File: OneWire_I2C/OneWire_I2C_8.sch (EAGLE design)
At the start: 17 parts

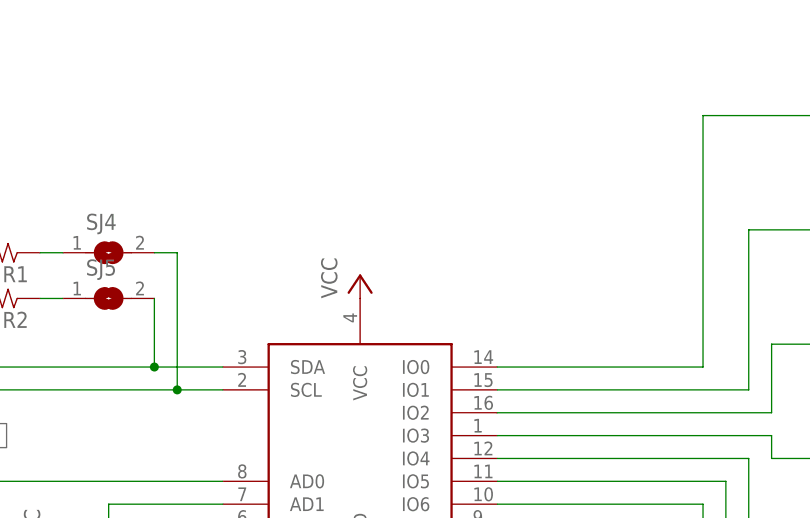
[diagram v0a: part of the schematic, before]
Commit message: Tweaks to I2C 1Wire bridge boards
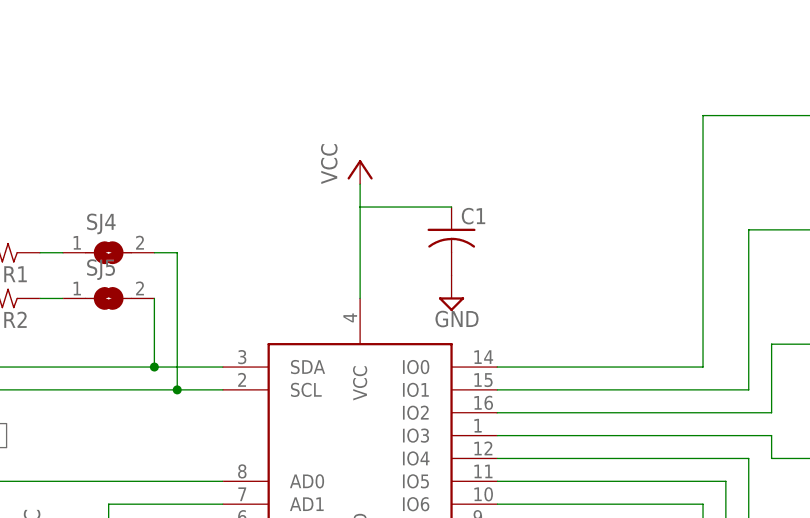
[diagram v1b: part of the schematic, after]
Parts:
- added C1: (no value), resistor:C-USC0603
- renumbered U$1 to W1
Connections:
- net GND: now also C1.2
- net VCC: now also C1.1
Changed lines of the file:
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@@
 <parts>
 <part name="FRAME1" library="frames" deviceset="LETTER_L" device=""/>
-<part name="U$1" library="Puffin" deviceset="DS2482-800" device=""/>
+<part name="W1" library="Puffin" deviceset="DS2482-800" device=""/>
 <part name="J1" library="SparkFun-Connectors" deviceset="M03" device="PTH"/>
 <part name="J2" library="SparkFun-Connectors" deviceset="M03" device="PTH"/>
@@
 <part name="SJ4" library="jumper" deviceset="SJ" device=""/>
 <part name="SJ5" library="jumper" deviceset="SJ" device=""/>
+<part name="C1" library="resistor" deviceset="C-US" device="C0603"/>
+<part name="SUPPLY2" library="supply2" deviceset="GND" device=""/>
 </parts>
 <sheets>
@@
 <instance part="FRAME1" gate="G$1" x="0" y="0"/>
 <instance part="FRAME1" gate="G$2" x="147.32" y="0"/>
-<instance part="U$1" gate="G$1" x="121.92" y="106.68"/>
+<instance part="W1" gate="G$1" x="121.92" y="106.68"/>
 <instance part="J1" gate="J$1" x="195.58" y="149.86" rot="R180"/>
 <instance part="J2" gate="J$1" x="195.58" y="137.16" rot="R180"/>
@@
 <instance part="SJ2" gate="G$1" x="81.28" y="88.9" rot="R270"/>
 <instance part="SJ3" gate="G$1" x="81.28" y="78.74" rot="R270"/>
-<instance part="VCC" gate="VCC" x="121.92" y="132.08"/>
+<instance part="VCC" gate="VCC" x="121.92" y="144.78"/>
 <instance part="P+2" gate="VCC" x="180.34" y="157.48"/>
 <instance part="P+3" gate="VCC" x="71.12" y="142.24"/>
@@
 <instance part="SJ4" gate="1" x="93.98" y="134.62"/>
 <instance part="SJ5" gate="1" x="93.98" y="129.54"/>
+<instance part="C1" gate="G$1" x="132.08" y="137.16"/>
+<instance part="SUPPLY2" gate="GND" x="132.08" y="129.54"/>
 </instances>
 <busses>
@@
 <net name="IO0" class="0">
 <segment>
-<pinref part="U$1" gate="G$1" pin="IO0"/>
+<pinref part="W1" gate="G$1" pin="IO0"/>
 <wire x1="137.16" y1="121.92" x2="160.02" y2="121.92" width="0.1524" layer="91"/>
 <wire x1="160.02" y1="121.92" x2="160.02" y2="149.86" width="0.1524" layer="91"/>
@@
 <net name="IO1" class="0">
 <segment>
-<pinref part="U$1" gate="G$1" pin="IO1"/>
+<pinref part="W1" gate="G$1" pin="IO1"/>
 <wire x1="137.16" y1="119.38" x2="165.1" y2="119.38" width="0.1524" layer="91"/>
 <wire x1="165.1" y1="119.38" x2="165.1" y2="137.16" width="0.1524" layer="91"/>
@@
 <net name="IO2" class="0">
 <segment>
-<pinref part="U$1" gate="G$1" pin="IO2"/>
+<pinref part="W1" gate="G$1" pin="IO2"/>
 <wire x1="137.16" y1="116.84" x2="167.64" y2="116.84" width="0.1524" layer="91"/>
 <wire x1="167.64" y1="116.84" x2="167.64" y2="124.46" width="0.1524" layer="91"/>
@@
 <net name="IO3" class="0">
 <segment>
-<pinref part="U$1" gate="G$1" pin="IO3"/>
+<pinref part="W1" gate="G$1" pin="IO3"/>
 <wire x1="137.16" y1="114.3" x2="167.64" y2="114.3" width="0.1524" layer="91"/>
 <wire x1="167.64" y1="114.3" x2="167.64" y2="111.76" width="0.1524" layer="91"/>
@@
 <net name="IO4" class="0">
 <segment>
-<pinref part="U$1" gate="G$1" pin="IO4"/>
+<pinref part="W1" gate="G$1" pin="IO4"/>
 <wire x1="137.16" y1="111.76" x2="165.1" y2="111.76" width="0.1524" layer="91"/>
 <wire x1="165.1" y1="111.76" x2="165.1" y2="99.06" width="0.1524" layer="91"/>
@@
 <net name="IO5" class="0">
 <segment>
-<pinref part="U$1" gate="G$1" pin="IO5"/>
+<pinref part="W1" gate="G$1" pin="IO5"/>
 <wire x1="137.16" y1="109.22" x2="162.56" y2="109.22" width="0.1524" layer="91"/>
 <wire x1="162.56" y1="109.22" x2="162.56" y2="86.36" width="0.1524" layer="91"/>
@@
 <net name="IO6" class="0">
 <segment>
-<pinref part="U$1" gate="G$1" pin="IO6"/>
+<pinref part="W1" gate="G$1" pin="IO6"/>
 <wire x1="137.16" y1="106.68" x2="160.02" y2="106.68" width="0.1524" layer="91"/>
 <wire x1="160.02" y1="106.68" x2="160.02" y2="73.66" width="0.1524" layer="91"/>
@@
 <net name="IO7" class="0">
 <segment>
-<pinref part="U$1" gate="G$1" pin="IO7"/>
+<pinref part="W1" gate="G$1" pin="IO7"/>
 <wire x1="137.16" y1="104.14" x2="157.48" y2="104.14" width="0.1524" layer="91"/>
 <wire x1="157.48" y1="104.14" x2="157.48" y2="60.96" width="0.1524" layer="91"/>
@@
 <net name="GND" class="0">
 <segment>
-<pinref part="U$1" gate="G$1" pin="GND"/>
+<pinref part="W1" gate="G$1" pin="GND"/>
 <pinref part="GND" gate="GND" pin="GND"/>
 </segment>
@@
 <junction x="182.88" y="58.42"/>
 </segment>
+<segment>
+<pinref part="C1" gate="G$1" pin="2"/>
+<pinref part="SUPPLY2" gate="GND" pin="GND"/>
+</segment>
 </net>
 <net name="VCC" class="0">
 <segment>
-<pinref part="U$1" gate="G$1" pin="VCC"/>
+<pinref part="W1" gate="G$1" pin="VCC"/>
 <pinref part="VCC" gate="VCC" pin="VCC"/>
+<wire x1="121.92" y1="142.24" x2="121.92" y2="139.7" width="0.1524" layer="91"/>
+<pinref part="C1" gate="G$1" pin="1"/>
+<wire x1="121.92" y1="139.7" x2="121.92" y2="129.54" width="0.1524" layer="91"/>
+<wire x1="132.08" y1="139.7" x2="121.92" y2="139.7" width="0.1524" layer="91"/>
 </segment>
 <segment>
@@
 <net name="AD0" class="0">
 <segment>
-<pinref part="U$1" gate="G$1" pin="AD0"/>
+<pinref part="W1" gate="G$1" pin="AD0"/>
 <pinref part="SJ1" gate="G$1" pin="2"/>
 <wire x1="106.68" y1="109.22" x2="81.28" y2="109.22" width="0.1524" layer="91"/>
@@
 <wire x1="81.28" y1="93.98" x2="93.98" y2="93.98" width="0.1524" layer="91"/>
 <wire x1="93.98" y1="93.98" x2="93.98" y2="106.68" width="0.1524" layer="91"/>
-<pinref part="U$1" gate="G$1" pin="AD1"/>
+<pinref part="W1" gate="G$1" pin="AD1"/>
 <wire x1="93.98" y1="106.68" x2="106.68" y2="106.68" width="0.1524" layer="91"/>
 </segment>
@@
 <wire x1="81.28" y1="83.82" x2="96.52" y2="83.82" width="0.1524" layer="91"/>
 <wire x1="96.52" y1="83.82" x2="96.52" y2="104.14" width="0.1524" layer="91"/>
-<pinref part="U$1" gate="G$1" pin="AD2"/>
+<pinref part="W1" gate="G$1" pin="AD2"/>
 <wire x1="96.52" y1="104.14" x2="106.68" y2="104.14" width="0.1524" layer="91"/>
 </segment>
@@
 <segment>
 <pinref part="J9" gate="G$1" pin="5"/>
-<pinref part="U$1" gate="G$1" pin="SDA"/>
+<pinref part="W1" gate="G$1" pin="SDA"/>
 <wire x1="66.04" y1="121.92" x2="99.06" y2="121.92" width="0.1524" layer="91"/>
 <pinref part="SJ5" gate="1" pin="2"/>
@@
 <segment>
 <pinref part="J9" gate="G$1" pin="4"/>
-<pinref part="U$1" gate="G$1" pin="SCL"/>
+<pinref part="W1" gate="G$1" pin="SCL"/>
 <wire x1="66.04" y1="119.38" x2="101.6" y2="119.38" width="0.1524" layer="91"/>
 <pinref part="SJ4" gate="1" pin="2"/>

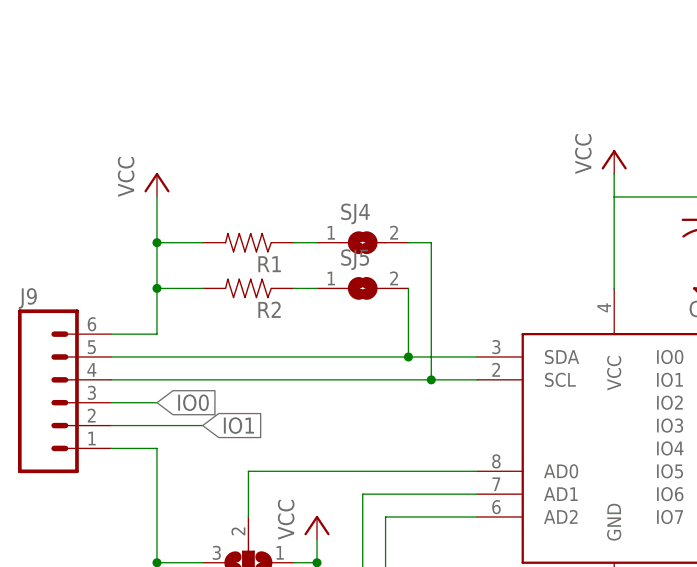
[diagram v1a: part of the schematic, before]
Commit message: Changed I2C pullup jumpers to single 3-way jumper
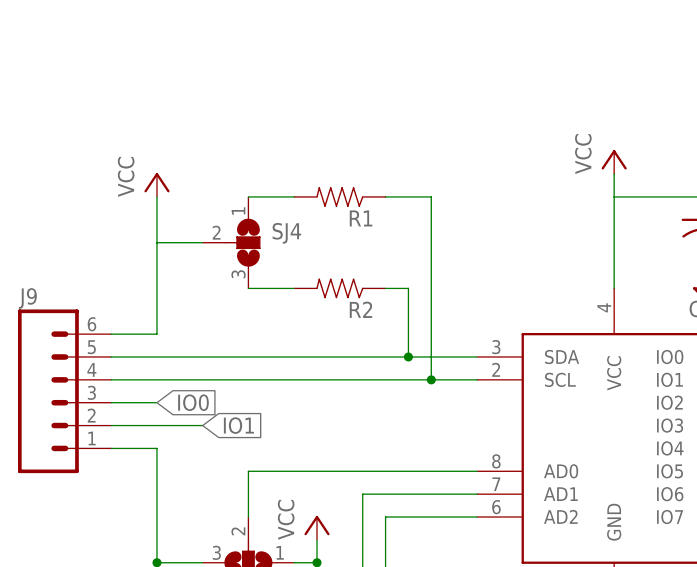
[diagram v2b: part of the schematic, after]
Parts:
- removed SJ5: (no value), jumper:SJ
- SJ4: device jumper:SJ -> jumper:SJ2W
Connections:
- net N$1: now also R1.2; no longer R1.1
- net N$2: now also R2.2, SJ4.3; no longer R2.1, SJ5.1
- net SCL: now also R1.1; no longer SJ4.2
- net SDA: now also R2.1; no longer SJ5.2
- net VCC: now also SJ4.2; no longer R1.2, R2.2
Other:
- moved on the sheet: R1, R2
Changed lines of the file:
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@@
 <part name="R1" library="SparkFun-Passives" deviceset="RESISTOR" device="0603-RES"/>
 <part name="R2" library="SparkFun-Passives" deviceset="RESISTOR" device="0603-RES"/>
-<part name="SJ4" library="jumper" deviceset="SJ" device=""/>
-<part name="SJ5" library="jumper" deviceset="SJ" device=""/>
 <part name="C1" library="resistor" deviceset="C-US" device="C0603"/>
 <part name="SUPPLY2" library="supply2" deviceset="GND" device=""/>
+<part name="SJ4" library="jumper" deviceset="SJ2W" device=""/>
 </parts>
 <sheets>
@@
 <instance part="P+3" gate="VCC" x="71.12" y="142.24"/>
 <instance part="P+4" gate="VCC" x="88.9" y="104.14"/>
-<instance part="R1" gate="G$1" x="81.28" y="134.62" rot="R180"/>
-<instance part="R2" gate="G$1" x="81.28" y="129.54" rot="R180"/>
-<instance part="SJ4" gate="1" x="93.98" y="134.62"/>
-<instance part="SJ5" gate="1" x="93.98" y="129.54"/>
+<instance part="R1" gate="G$1" x="91.44" y="139.7" rot="R180"/>
+<instance part="R2" gate="G$1" x="91.44" y="129.54" rot="R180"/>
 <instance part="C1" gate="G$1" x="132.08" y="137.16"/>
 <instance part="SUPPLY2" gate="GND" x="132.08" y="129.54"/>
+<instance part="SJ4" gate="G$1" x="81.28" y="134.62"/>
 </instances>
 <busses>
@@
 <pinref part="P+3" gate="VCC" pin="VCC"/>
 <wire x1="66.04" y1="124.46" x2="71.12" y2="124.46" width="0.1524" layer="91"/>
-<wire x1="71.12" y1="124.46" x2="71.12" y2="129.54" width="0.1524" layer="91"/>
-<pinref part="R2" gate="G$1" pin="2"/>
-<wire x1="71.12" y1="129.54" x2="71.12" y2="134.62" width="0.1524" layer="91"/>
+<wire x1="71.12" y1="124.46" x2="71.12" y2="134.62" width="0.1524" layer="91"/>
+<pinref part="SJ4" gate="G$1" pin="2"/>
 <wire x1="71.12" y1="134.62" x2="71.12" y2="139.7" width="0.1524" layer="91"/>
-<wire x1="76.2" y1="129.54" x2="71.12" y2="129.54" width="0.1524" layer="91"/>
-<pinref part="R1" gate="G$1" pin="2"/>
 <wire x1="76.2" y1="134.62" x2="71.12" y2="134.62" width="0.1524" layer="91"/>
-<junction x="71.12" y="134.62"/>
-<junction x="71.12" y="129.54"/>
 </segment>
 <segment>
@@
 <pinref part="W1" gate="G$1" pin="SDA"/>
 <wire x1="66.04" y1="121.92" x2="99.06" y2="121.92" width="0.1524" layer="91"/>
-<pinref part="SJ5" gate="1" pin="2"/>
 <wire x1="99.06" y1="121.92" x2="106.68" y2="121.92" width="0.1524" layer="91"/>
 <wire x1="99.06" y1="129.54" x2="99.06" y2="121.92" width="0.1524" layer="91"/>
 <junction x="99.06" y="121.92"/>
+<pinref part="R2" gate="G$1" pin="1"/>
+<wire x1="96.52" y1="129.54" x2="99.06" y2="129.54" width="0.1524" layer="91"/>
 </segment>
 </net>
@@
 <pinref part="W1" gate="G$1" pin="SCL"/>
 <wire x1="66.04" y1="119.38" x2="101.6" y2="119.38" width="0.1524" layer="91"/>
-<pinref part="SJ4" gate="1" pin="2"/>
 <wire x1="101.6" y1="119.38" x2="106.68" y2="119.38" width="0.1524" layer="91"/>
-<wire x1="99.06" y1="134.62" x2="101.6" y2="134.62" width="0.1524" layer="91"/>
-<wire x1="101.6" y1="134.62" x2="101.6" y2="119.38" width="0.1524" layer="91"/>
+<wire x1="96.52" y1="139.7" x2="101.6" y2="139.7" width="0.1524" layer="91"/>
+<wire x1="101.6" y1="139.7" x2="101.6" y2="119.38" width="0.1524" layer="91"/>
 <junction x="101.6" y="119.38"/>
+<pinref part="R1" gate="G$1" pin="1"/>
 </segment>
 </net>
 <net name="N$1" class="0">
 <segment>
-<pinref part="R1" gate="G$1" pin="1"/>
-<pinref part="SJ4" gate="1" pin="1"/>
-<wire x1="86.36" y1="134.62" x2="88.9" y2="134.62" width="0.1524" layer="91"/>
+<pinref part="SJ4" gate="G$1" pin="1"/>
+<pinref part="R1" gate="G$1" pin="2"/>
+<wire x1="81.28" y1="139.7" x2="86.36" y2="139.7" width="0.1524" layer="91"/>
 </segment>
 </net>
 <net name="N$2" class="0">
 <segment>
-<pinref part="R2" gate="G$1" pin="1"/>
-<pinref part="SJ5" gate="1" pin="1"/>
-<wire x1="86.36" y1="129.54" x2="88.9" y2="129.54" width="0.1524" layer="91"/>
-</segment>
-</net>
+<pinref part="SJ4" gate="G$1" pin="3"/>
+<pinref part="R2" gate="G$1" pin="2"/>
+<wire x1="81.28" y1="129.54" x2="86.36" y2="129.54" width="0.1524" layer="91"/>
+</segment>
+</net>

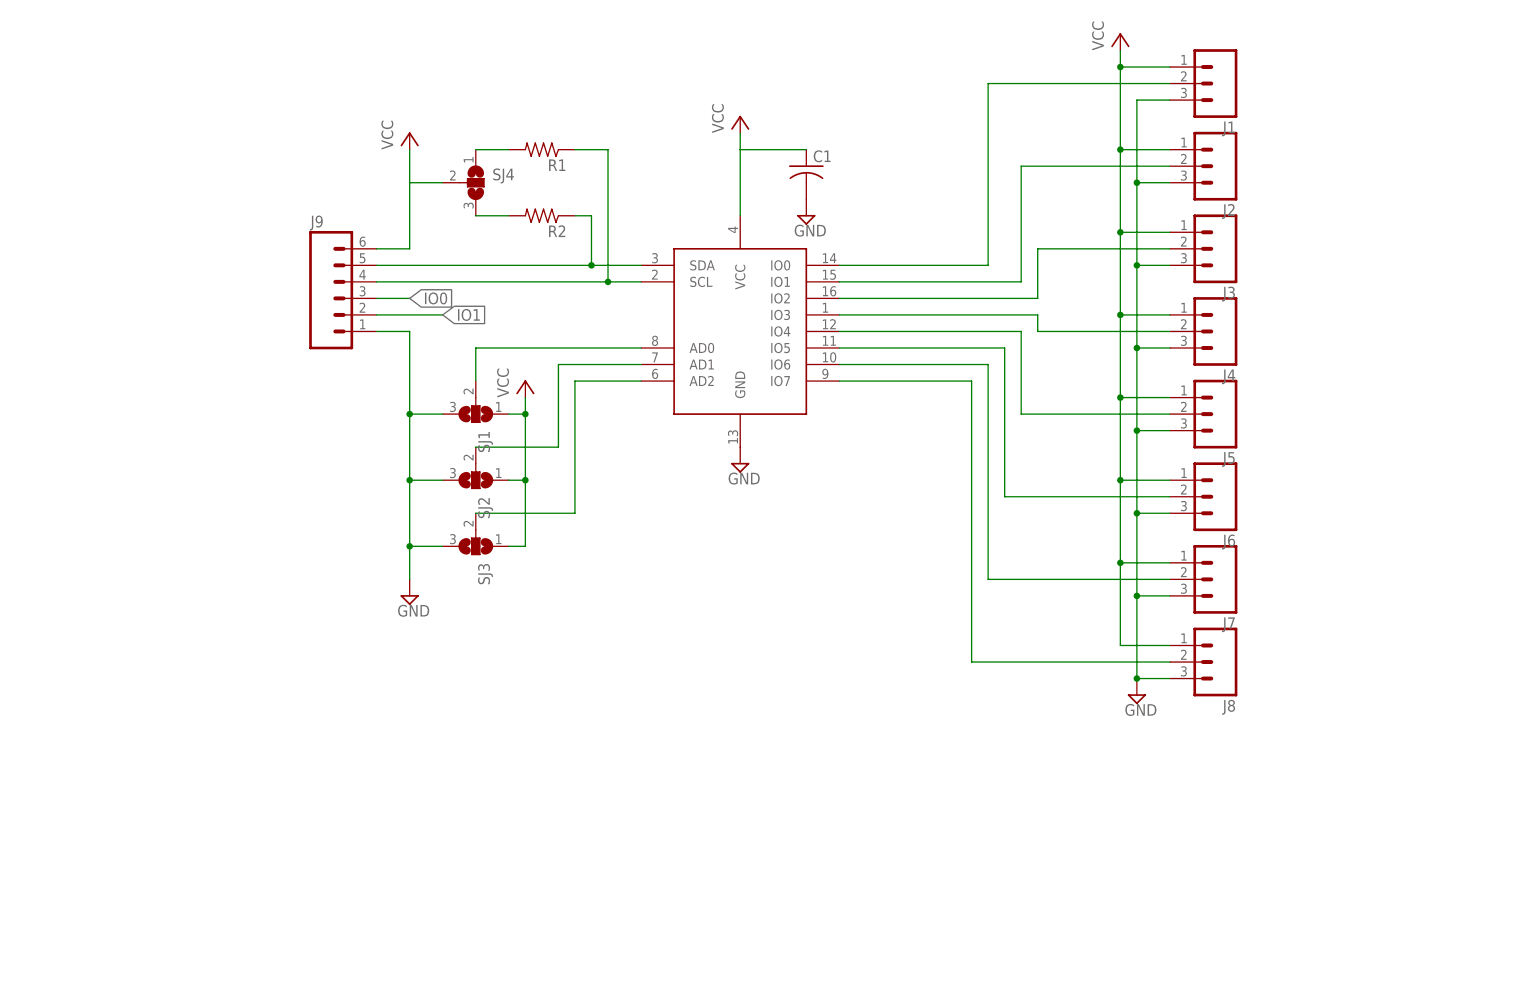
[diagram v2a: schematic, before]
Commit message: Added 8 port OneWire I2C bridge with Extender
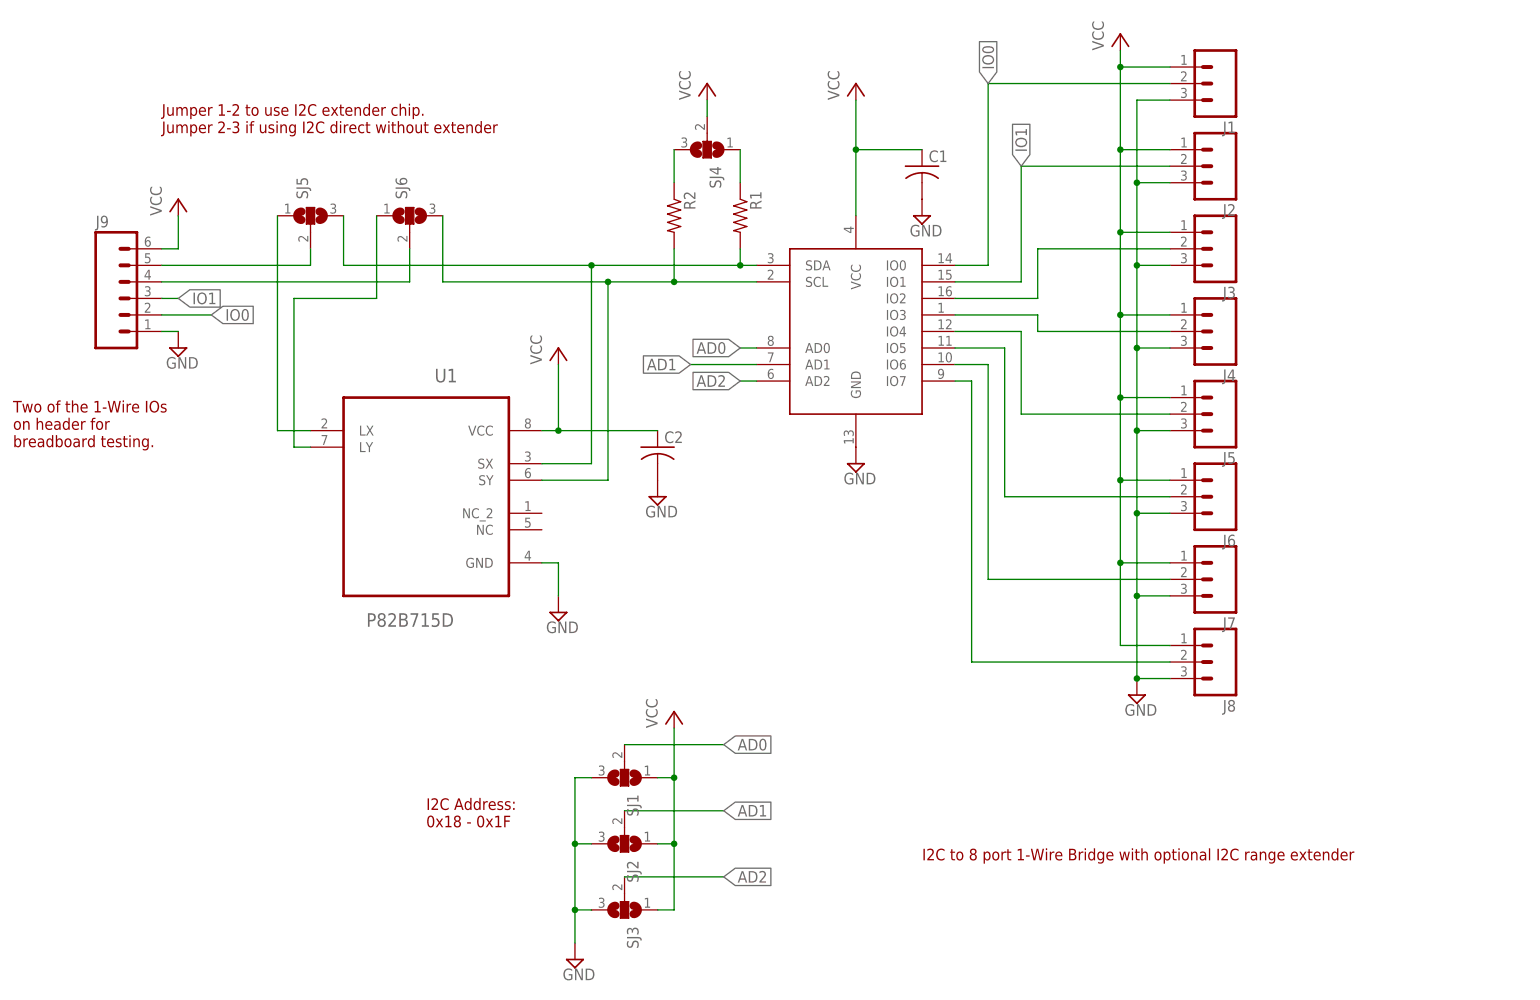
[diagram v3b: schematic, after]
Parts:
- added C2: (no value), resistor:C-USC0603
- added SJ5, SJ6: (no value), jumper:SJ2W
- added U1: P82B715D, Texas Instruments_By_element14_Batch_1:P82B715D
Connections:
- new net LSCL: J9.4, SJ6.2
- new net LSDA: J9.5, SJ5.2
- new net LX: SJ5.1, U1.LX
- new net LY: SJ6.1, U1.LY
- net GND: now also C2.2, U1.GND
- net IO0: now also J9.2; no longer J9.3
- net IO1: now also J9.3; no longer J9.2
- net N$1: now also R2.1, SJ4.3; no longer R1.2, SJ4.1
- net N$2: now also R1.1, SJ4.1; no longer R2.2, SJ4.3
- net SCL: now also R2.2, SJ6.3, U1.SY; no longer J9.4, R1.1
- net SDA: now also R1.2, SJ5.3, U1.SX; no longer J9.5, R2.1
- net VCC: now also C2.1, U1.VCC
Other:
- note added: "I2C Address: 0x18 - 0x1F"
- note added: "I2C to 8 port 1-Wire Bridge with optional I2C range extender"
- note added: "Jumper 1-2 to use I2C extender chip. Jumper 2-3 if using I2C direct without extender"
- note added: "Two of the 1-Wire IOs on header for breadboard testing."
- moved on the sheet: C1, J9, R1, R2, SJ1, SJ2, SJ3, SJ4
